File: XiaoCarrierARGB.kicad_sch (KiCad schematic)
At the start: 24 parts, among them J1 V_{IN}^{10-24V}, J2 Conn_01x08, J3 Conn_01x01, J4 Conn_01x08, J5 Conn_01x01, J6 Conn_01x06, U1 TLV75733PDBV, U2 TPP362083-T6TR, U3 XIAO-ESP32-C6-DIP, U4 74LVC1T45W6-7, U5 74LVC1T45W6-7, U6 74LVC1T45W6-7

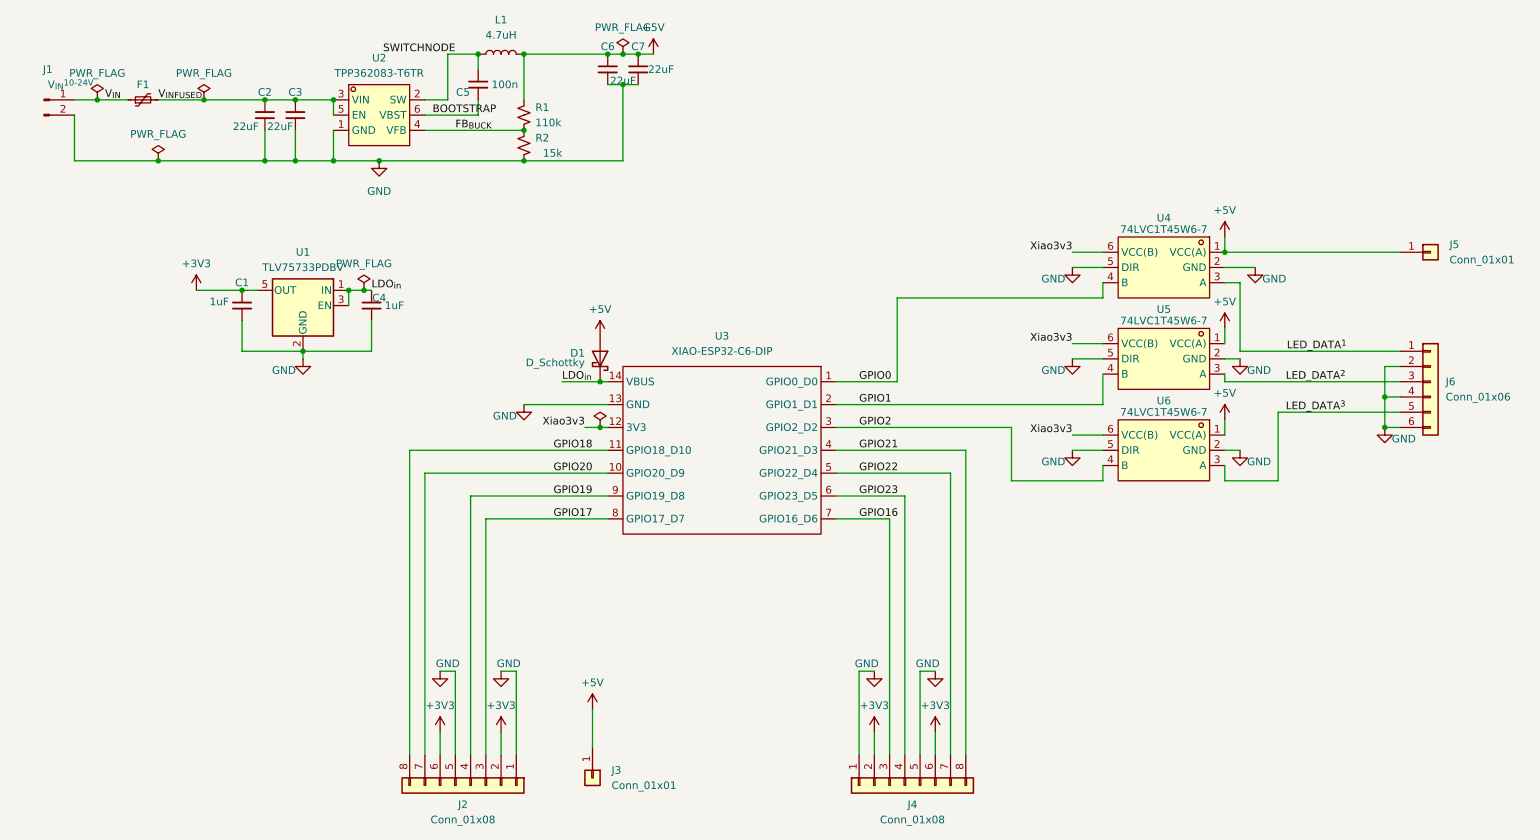
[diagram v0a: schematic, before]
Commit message: added jumpers and Rs for possible pullup pulldown on gpio also added r to data out lines to allow for compensation in long data lines
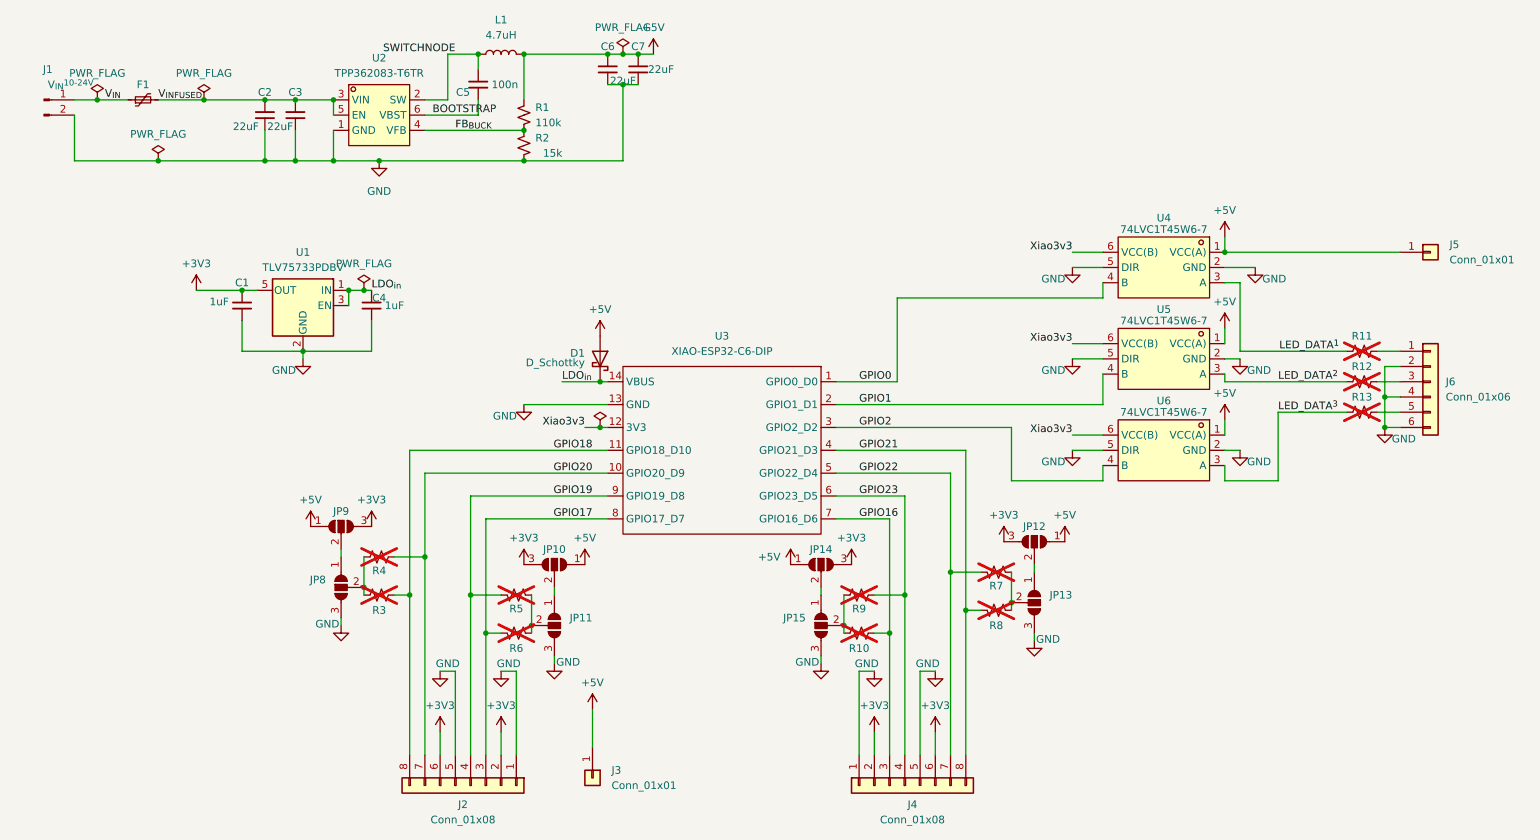
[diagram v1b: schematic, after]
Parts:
- added JP10, JP11, JP12, JP13, JP14, JP15, JP8, JP9: SolderJumper_3_Open, Jumper:SolderJumper-3_P1.3mm_Open_Pad1.0x1.5mm, symbol Jumper:SolderJumper_3_Open
- added R10, R11, R12, R13, R3, R4, R5, R6, R7, R8, R9: R_Small_US, Resistor_SMD:R_0805_2012Metric, symbol Device:R_Small_US
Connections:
- net +3V3: now also JP10.3 (B), JP12.3 (B), JP14.3 (B), JP9.3 (B)
- net +5V: now also JP10.1 (A), JP12.1 (A), JP14.1 (A), JP9.1 (A)
- net GND: now also JP11.3 (B), JP13.3 (B), JP15.3 (B), JP8.3 (B)
- net GPIO16: now also R10.2
- net GPIO17: now also R6.2
- net GPIO18: now also R3.2
- net GPIO19: now also R5.2
- net GPIO20: now also R4.2
- net GPIO21: now also R8.2
- net GPIO22: now also R7.2
- net GPIO23: now also R9.2
- net LED_DATA^{1}: now also R11.1; no longer J6.1 (Pin_1)
- net LED_DATA^{2}: now also R12.1; no longer J6.3 (Pin_3)
- net LED_DATA^{3}: now also R13.1; no longer J6.5 (Pin_5)
- new net: JP15.2 (C), R10.1, R9.1
- new net: JP11.2 (C), R5.1, R6.1
- new net: JP13.2 (C), R7.1, R8.1
- new net: J6.3 (Pin_3), R12.2
- new net: JP14.2 (C), JP15.1 (A)
- new net: J6.5 (Pin_5), R13.2
- new net: JP10.2 (C), JP11.1 (A)
- new net: JP12.2 (C), JP13.1 (A)
- new net: JP8.1 (A), JP9.2 (C)
- new net: JP8.2 (C), R3.1, R4.1
- new net: J6.1 (Pin_1), R11.2

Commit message: Refactored layout, added jumpers and unpopulated pull up/down Rs to backside of board
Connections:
- net +3V3: now also J4.3 (Pin_3), J4.7 (Pin_7); no longer J4.2 (Pin_2), J4.6 (Pin_6)
- net GND: now also J4.4 (Pin_4), J4.8 (Pin_8); no longer J4.1 (Pin_1), J4.5 (Pin_5)
- net GPIO16: now also J4.6 (Pin_6); no longer J4.3 (Pin_3)
- net GPIO21: now also J4.1 (Pin_1); no longer J4.8 (Pin_8)
- net GPIO22: now also J4.2 (Pin_2); no longer J4.7 (Pin_7)
- net GPIO23: now also J4.5 (Pin_5); no longer J4.4 (Pin_4)
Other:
- moved on the sheet: J4
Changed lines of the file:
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@@
 	(symbol
 		(lib_id "Connector_Generic:Conn_01x08")
-		(at 158.75 154.94 90)
-		(mirror x)
+		(at 161.29 154.94 270)
 		(unit 1)
 		(body_style 1)
@@
 		(in_pos_files yes)
 		(dnp no)
-		(fields_autoplaced yes)
 		(property "Reference" "J4"
 			(at 160.02 158.115 90)
@@
 		)
 		(property "Footprint" "Connector_PinHeader_2.54mm:PinHeader_1x08_P2.54mm_Vertical"
-			(at 158.75 154.94 0)
+			(at 161.29 154.94 0)
 			(hide yes)
 			(show_name no)
@@
 		)
 		(property "Datasheet" ""
-			(at 158.75 154.94 0)
+			(at 161.29 154.94 0)
 			(hide yes)
 			(show_name no)
@@
 		)
 		(property "Description" "Generic connector, single row, 01x08, script generated (kicad-library-utils/schlib/autogen/connector/)"
-			(at 158.75 154.94 0)
+			(at 161.29 154.94 0)
 			(hide yes)
 			(show_name no)

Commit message: Finished up layout
Need to do final sanity checks BUCK and such
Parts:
- added C8: 100n, Capacitor_SMD:C_0805_2012Metric_Pad1.18x1.45mm_HandSolder, symbol Device:C_Small
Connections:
- net GND: now also C8.1
- net LED_DATA^{1}: now also R11.2; no longer R11.1
- net LED_DATA^{2}: now also R12.2; no longer R12.1
- net LED_DATA^{3}: now also R13.2; no longer R13.1
- net V_{IN}_{FUSED}: now also C8.2
- net at J6.3 (Pin_3): now also R12.1; no longer R12.2
- net at J6.5 (Pin_5): now also R13.1; no longer R13.2
- net at J6.1 (Pin_1): now also R11.1; no longer R11.2
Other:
- moved on the sheet: R11, R12, R13
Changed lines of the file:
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@@
 	)
 	(junction
+		(at 44.45 50.8)
+		(diameter 0)
+		(color 0 0 0 0)
+	)
+	(junction
 		(at 24.13 40.64)
 		(diameter 0)
@@
 	)
 	(junction
+		(at 44.45 40.64)
+		(diameter 0)
+		(color 0 0 0 0)
+	)
+	(junction
 		(at 58.42 82.55)
 		(diameter 0)
@@
 	)
 	(junction
-		(at 34.29 50.8)
+		(at 33.02 50.8)
 		(diameter 0)
 		(color 0 0 0 0)
@@
 	(wire
 		(pts
-			(xy 237.49 82.55) (xy 241.3 82.55)
+			(xy 44.45 50.8) (xy 52.07 50.8)
 		)
 		(stroke
@@
 	(wire
 		(pts
-			(xy 186.69 81.28) (xy 191.77 81.28)
+			(xy 237.49 82.55) (xy 241.3 82.55)
 		)
 		(stroke
@@
 	(wire
 		(pts
-			(xy 163.83 135.89) (xy 161.29 135.89)
+			(xy 186.69 81.28) (xy 191.77 81.28)
 		)
 		(stroke
@@
 	(wire
 		(pts
-			(xy 212.09 87.63) (xy 232.41 87.63)
+			(xy 163.83 135.89) (xy 161.29 135.89)
 		)
 		(stroke
@@
 	(wire
 		(pts
-			(xy 48.26 82.55) (xy 58.42 82.55)
+			(xy 212.09 87.63) (xy 232.41 87.63)
 		)
 		(stroke
@@
 	(wire
 		(pts
-			(xy 73.66 123.19) (xy 76.2 123.19)
+			(xy 48.26 82.55) (xy 58.42 82.55)
 		)
 		(stroke
@@
 	(wire
 		(pts
-			(xy 57.15 40.64) (xy 63.5 40.64)
+			(xy 73.66 123.19) (xy 76.2 123.19)
 		)
 		(stroke
@@
 	(wire
 		(pts
-			(xy 34.29 50.8) (xy 52.07 50.8)
+			(xy 57.15 40.64) (xy 63.5 40.64)
 		)
 		(stroke
@@
 	(wire
 		(pts
+			(xy 44.45 45.72) (xy 44.45 50.8)
+		)
+		(stroke
+			(width 0)
+			(type default)
+		)
+	)
+	(wire
+		(pts
 			(xy 111.76 38.1) (xy 114.3 38.1)
 		)
@@
 	(wire
 		(pts
-			(xy 20.32 50.8) (xy 34.29 50.8)
+			(xy 20.32 50.8) (xy 44.45 50.8)
 		)
 		(stroke
@@
 	(wire
 		(pts
-			(xy 41.91 40.64) (xy 52.07 40.64)
+			(xy 41.91 40.64) (xy 44.45 40.64)
 		)
 		(stroke
@@
 	(wire
 		(pts
+			(xy 44.45 40.64) (xy 52.07 40.64)
+		)
+		(stroke
+			(width 0)
+			(type default)
+		)
+	)
+	(wire
+		(pts
 			(xy 48.26 77.47) (xy 48.26 82.55)
 		)
@@
 	(symbol
 		(lib_id "power:PWR_FLAG")
-		(at 34.29 50.8 0)
+		(at 33.02 50.8 0)
 		(unit 1)
 		(body_style 1)
@@
 		(fields_autoplaced yes)
 		(property "Reference" "#FLG03"
-			(at 34.29 48.895 0)
+			(at 33.02 48.895 0)
 			(hide yes)
 			(show_name no)
@@
 		)
 		(property "Value" "PWR_FLAG"
-			(at 34.29 46.355 0)
+			(at 33.02 46.355 0)
 			(show_name no)
 			(do_not_autoplace no)
@@
 		)
 		(property "Footprint" ""
-			(at 34.29 50.8 0)
+			(at 33.02 50.8 0)
 			(hide yes)
 			(show_name no)
@@
 		)
 		(property "Datasheet" ""
-			(at 34.29 50.8 0)
+			(at 33.02 50.8 0)
 			(hide yes)
 			(show_name no)
@@
 		)
 		(property "Description" "Special symbol for telling ERC where power comes from"
-			(at 34.29 50.8 0)
+			(at 33.02 50.8 0)
 			(hide yes)
 			(show_name no)
@@
 	(symbol
 		(lib_id "Device:R_Small_US")
-		(at 234.95 87.63 90)
+		(at 234.95 87.63 270)
+		(mirror x)
 		(unit 1)
 		(body_style 1)
@@
 	(symbol
 		(lib_id "Device:R_Small_US")
-		(at 234.95 92.71 90)
+		(at 234.95 92.71 270)
+		(mirror x)
 		(unit 1)
 		(body_style 1)
@@
 	(symbol
 		(lib_id "Device:R_Small_US")
-		(at 234.95 82.55 90)
+		(at 234.95 82.55 270)
+		(mirror x)
 		(unit 1)
 		(body_style 1)
@@
 					(unit 1)
 				)
+			)
+		)
+	)
+	(symbol
+		(lib_id "Device:C_Small")
+		(at 44.45 43.18 180)
+		(unit 1)
+		(body_style 1)
+		(exclude_from_sim no)
+		(in_bom yes)
+		(on_board yes)
+		(in_pos_files yes)
+		(dnp no)
+		(property "Reference" "C8"
+			(at 44.45 39.37 0)
+			(show_name no)
+			(do_not_autoplace no)
+			(effects
+				(font
+					(size 1.27 1.27)
+				)
+			)
+		)
+		(property "Value" "100n"
+			(at 40.64 45.72 0)
+			(show_name no)
+			(do_not_autoplace no)
+			(effects
+				(font
+					(size 1.27 1.27)
+				)
+			)
+		)
+		(property "Footprint" "Capacitor_SMD:C_0805_2012Metric_Pad1.18x1.45mm_HandSolder"
+			(at 44.45 43.18 0)
+			(hide yes)
+			(show_name no)
+			(do_not_autoplace no)
+			(effects
+				(font
+					(size 1.27 1.27)
+				)
+			)
+		)
+		(property "Datasheet" ""
+			(at 44.45 43.18 0)
+			(hide yes)
+			(show_name no)
+			(do_not_autoplace no)
+			(effects
+				(font
+					(size 1.27 1.27)
+				)
+			)
+		)
+		(property "Description" "Unpolarized capacitor, small symbol"
+			(at 44.45 33.02 0)
+			(hide yes)
+			(show_name no)
+			(do_not_autoplace no)
+			(effects
+				(font
+					(size 1.27 1.27)
+				)
+			)
+		)
+		(pin "1"
+		)
+		(pin "2"
+		)
+		(instances
+			(project "XiaoCarrierARGB"
+				(path "/e1106a3e-58d8-419c-bcd2-ced17f637917"
+					(reference "C8")
+					(unit 1)
+				)

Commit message: generated gerbers and ibom
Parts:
- U1: DigiKey Part (none) -> 296-50414; LCSC Part (none) -> C485517; MPN (none) -> TLV75733PDBVR
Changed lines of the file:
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@@
+			)
+		)
+		(property "MPN" "TLV75733PDBVR"
+			(at 58.42 74.93 0)
+			(hide yes)
+			(show_name no)
+			(do_not_autoplace no)
+			(effects
+				(font
+					(size 1.27 1.27)
+				)
+			)
+		)
+		(property "DigiKey Part" "296-50414"
+			(at 58.42 74.93 0)
+			(hide yes)
+			(show_name no)
+			(do_not_autoplace no)
+			(effects
+				(font
+					(size 1.27 1.27)
+				)
+			)
+		)
+		(property "LCSC Part" "C485517"
+			(at 58.42 74.93 0)
+			(hide yes)
+			(show_name no)
+			(do_not_autoplace no)
+			(effects
+				(font
+					(size 1.27 1.27)
+				)
 			)
 		)

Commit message: ReExport BOM
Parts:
- C5, C8: value 100n -> 100nF
